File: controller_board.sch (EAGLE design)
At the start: 44 parts, among them J1 FRSKY-GIMBAL, J12 JST_3PIN_GND_VDD_SIG, J14 JST_3PIN_GND_VDD_SIG, J16 JST_3PIN_GND_VDD_SIG, J18 JST_3PIN_GND_VDD_SIG, J2 FRSKY-GIMBAL, J3 WIRE-HARNESS-SPARKFUN-9915, J6 HEADER-0.1IN-6POS-SCREW, J7 HEADER-0.1IN-6POS-FEMALE

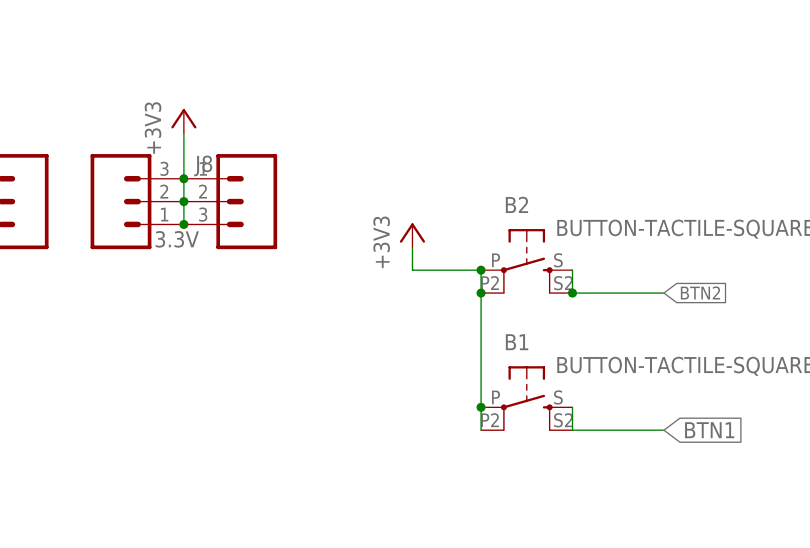
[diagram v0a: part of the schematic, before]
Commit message: fix polarity on butons.  Connect unconnected pin on batgnd breakouts
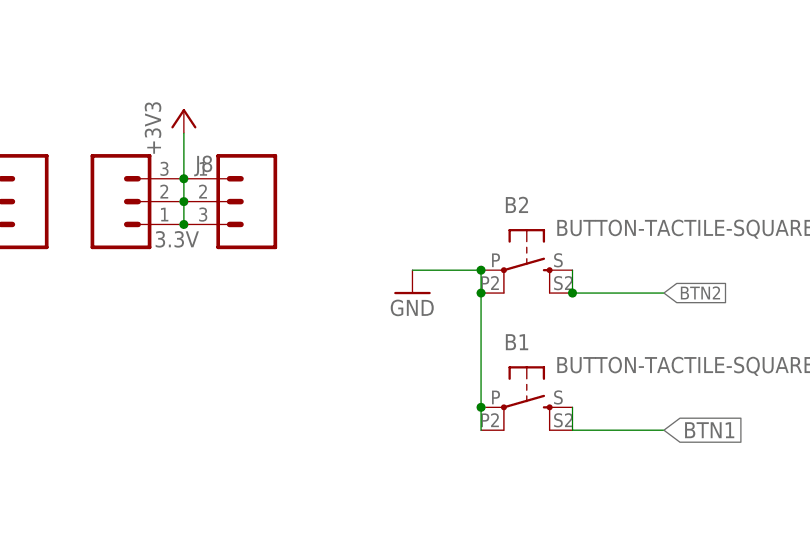
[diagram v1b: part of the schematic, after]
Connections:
- net +3V3: no longer B1.P, B1.P1, B2.P, B2.P1
- net GND: now also B1.P, B1.P1, B2.P, B2.P1
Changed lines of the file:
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@@
 <part name="D1" library="Components" deviceset="LED" device="3MM"/>
 <part name="B2" library="Controller" deviceset="BUTTON-TACTILE" device="-SQUARE"/>
-<part name="+3V6" library="supply1" deviceset="+3V3" device=""/>
 <part name="GND" library="Components" deviceset="HEADER-0.1IN-3POS" device="-SCREW">
 <attribute name="PIN1" value=""/>
@@
 <part name="GND9" library="supply1" deviceset="GND" device=""/>
 <part name="GND12" library="supply1" deviceset="GND" device=""/>
+<part name="GND10" library="supply1" deviceset="GND" device=""/>
 </parts>
 <sheets>
@@
 <instance part="D1" gate="G$1" x="-22.86" y="-17.78"/>
 <instance part="B2" gate="G$1" x="86.36" y="124.46" rot="R270"/>
-<instance part="+3V6" gate="G$1" x="73.66" y="129.54"/>
 <instance part="GND" gate="G$1" x="-15.24" y="127"/>
 <instance part="VBAT" gate="G$1" x="12.7" y="127"/>
@@
 <instance part="GND9" gate="1" x="167.64" y="17.78"/>
 <instance part="GND12" gate="1" x="157.48" y="17.78"/>
+<instance part="GND10" gate="1" x="73.66" y="121.92"/>
 </instances>
 <busses>
@@
 <wire x1="157.48" y1="30.48" x2="157.48" y2="20.32" width="0.1524" layer="91"/>
 </segment>
+<segment>
+<pinref part="B1" gate="G$1" pin="P1"/>
+<pinref part="B2" gate="G$1" pin="P1"/>
+<pinref part="B2" gate="G$1" pin="P"/>
+<wire x1="81.28" y1="124.46" x2="81.28" y2="121.92" width="0.1524" layer="91"/>
+<junction x="81.28" y="121.92"/>
+<pinref part="B1" gate="G$1" pin="P"/>
+<wire x1="81.28" y1="109.22" x2="81.28" y2="121.92" width="0.1524" layer="91"/>
+<junction x="81.28" y="109.22"/>
+<wire x1="81.28" y1="109.22" x2="81.28" y2="106.68" width="0.1524" layer="91"/>
+<wire x1="81.28" y1="124.46" x2="73.66" y2="124.46" width="0.1524" layer="91"/>
+<junction x="81.28" y="124.46"/>
+<pinref part="GND10" gate="1" pin="GND"/>
+</segment>
 </net>
 <net name="BTN1" class="0">
@@
 </segment>
 <segment>
-<pinref part="B1" gate="G$1" pin="P1"/>
-<pinref part="B2" gate="G$1" pin="P1"/>
-<pinref part="B2" gate="G$1" pin="P"/>
-<wire x1="81.28" y1="124.46" x2="81.28" y2="121.92" width="0.1524" layer="91"/>
-<junction x="81.28" y="121.92"/>
-<pinref part="B1" gate="G$1" pin="P"/>
-<wire x1="81.28" y1="109.22" x2="81.28" y2="121.92" width="0.1524" layer="91"/>
-<junction x="81.28" y="109.22"/>
-<wire x1="81.28" y1="109.22" x2="81.28" y2="106.68" width="0.1524" layer="91"/>
-<wire x1="81.28" y1="124.46" x2="73.66" y2="124.46" width="0.1524" layer="91"/>
-<junction x="81.28" y="124.46"/>
-<wire x1="73.66" y1="124.46" x2="73.66" y2="127" width="0.1524" layer="91"/>
-<pinref part="+3V6" gate="G$1" pin="+3V3"/>
-</segment>
-<segment>

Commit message: fix polarity on butons.  Connect unconnected pin on batgnd breakouts
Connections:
- net BATGND: now also GND.2
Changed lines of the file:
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@@
 <pinref part="J10" gate="G$1" pin="3"/>
 <label x="-5.08" y="124.46" size="1.778" layer="95" rot="R270" xref="yes"/>
+<pinref part="GND" gate="G$1" pin="2"/>
 </segment>
 <segment>

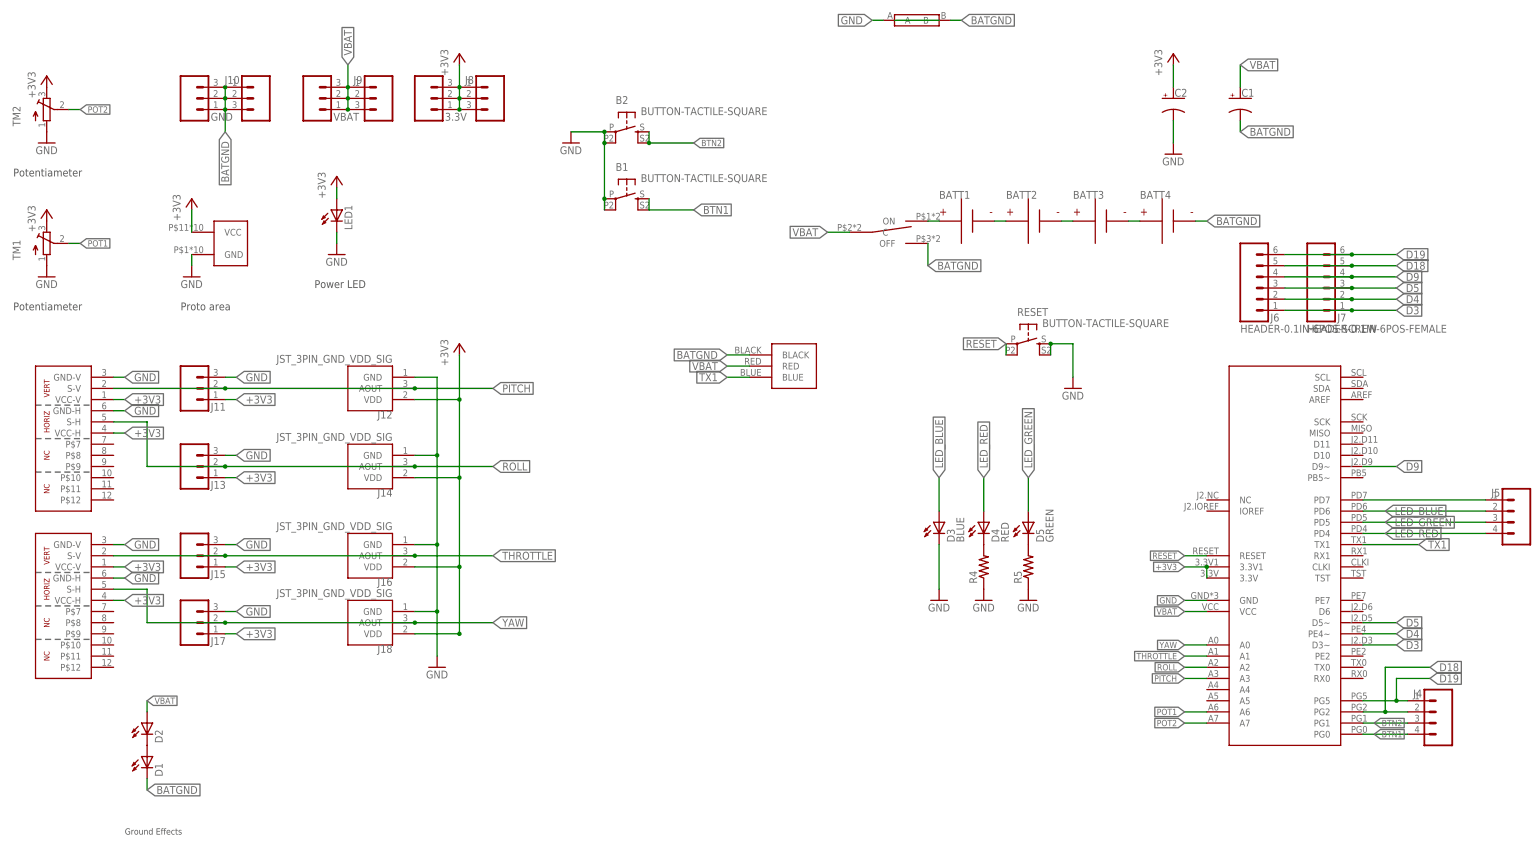
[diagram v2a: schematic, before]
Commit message: Connect AREF to 3.3V
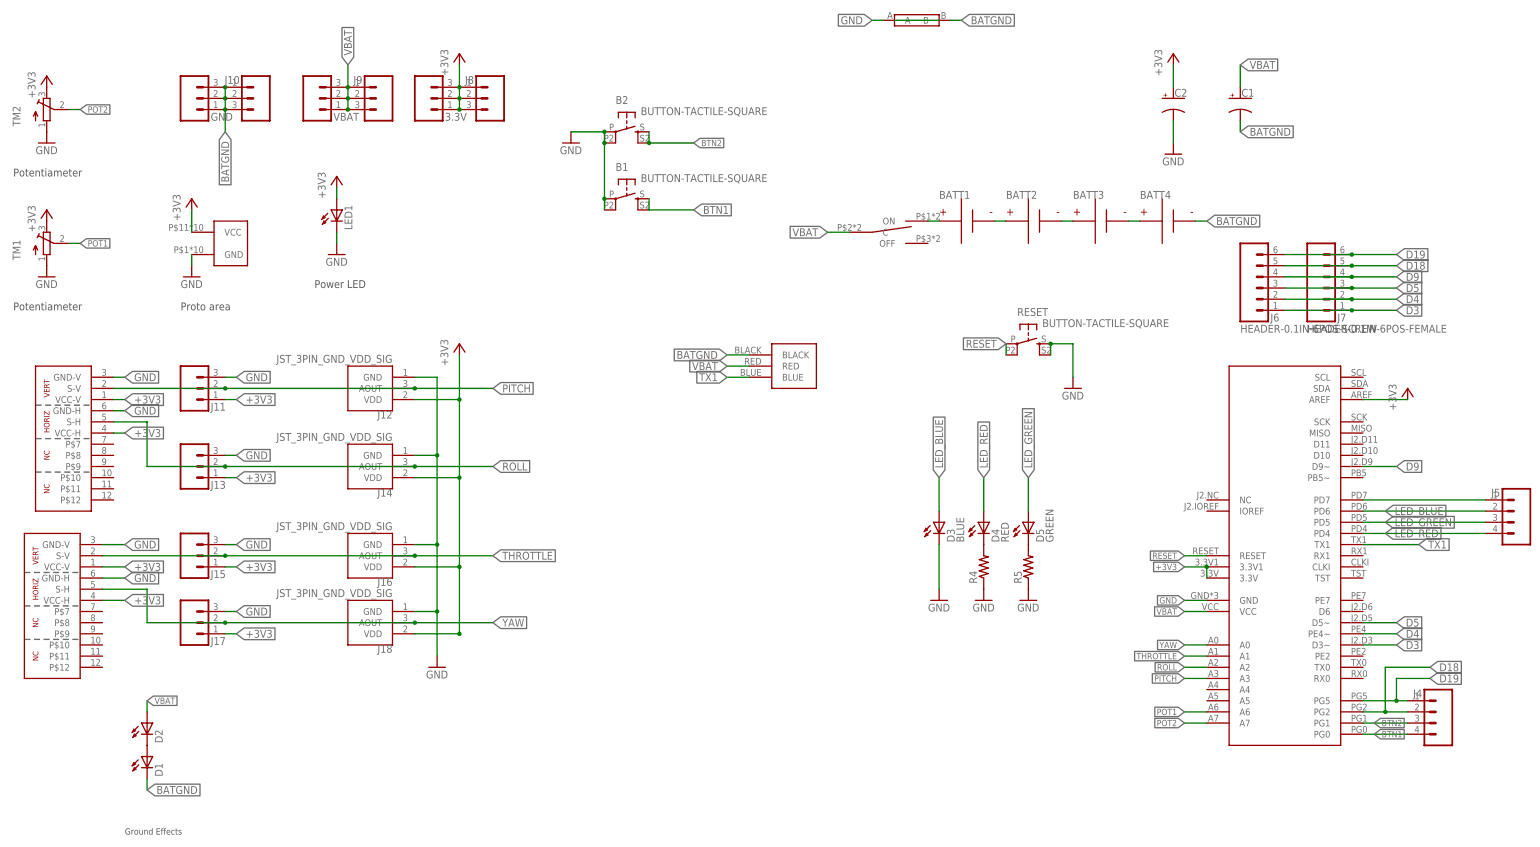
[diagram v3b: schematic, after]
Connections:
- net +3V3: now also U$4.AREF
- net BATGND: no longer S1.OFF
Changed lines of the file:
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@@
 <layer number="112" name="tSilk" color="7" fill="1" visible="yes" active="yes"/>
 <layer number="113" name="IDFDebug" color="4" fill="1" visible="yes" active="yes"/>
-<layer number="114" name="Unresolved" color="12" fill="1" visible="yes" active="yes"/>
-<layer number="115" name="Resolved" color="10" fill="1" visible="yes" active="yes"/>
-<layer number="116" name="Generic" color="9" fill="1" visible="yes" active="yes"/>
+<layer number="114" name="Unresolved" color="12" fill="1" visible="no" active="yes"/>
+<layer number="115" name="Resolved" color="10" fill="1" visible="no" active="yes"/>
+<layer number="116" name="Generic" color="9" fill="1" visible="no" active="yes"/>
 <layer number="11" name="Route11" color="4" fill="7" visible="no" active="no"/>
 <layer number="12" name="Route12" color="1" fill="5" visible="no" active="no"/>
@@
 <part name="GND12" library="supply1" deviceset="GND" device=""/>
 <part name="GND10" library="supply1" deviceset="GND" device=""/>
+<part name="+3V6" library="supply1" deviceset="+3V3" device=""/>
 </parts>
 <sheets>
@@
 <instance part="J15" gate="G$1" x="-15.24" y="22.86"/>
 <instance part="J17" gate="G$1" x="-15.24" y="7.62"/>
-<instance part="J2" gate="G$1" x="-33.02" y="5.08">
-<attribute name="CH1" x="-33.02" y="5.08" size="1.4224" layer="96" display="off"/>
-<attribute name="CH2" x="-33.02" y="5.08" size="1.4224" layer="96" display="off"/>
+<instance part="J2" gate="G$1" x="-35.56" y="5.08">
+<attribute name="CH1" x="-35.56" y="5.08" size="1.4224" layer="96" display="off"/>
+<attribute name="CH2" x="-35.56" y="5.08" size="1.4224" layer="96" display="off"/>
 </instance>
 <instance part="J1" gate="G$1" x="-33.02" y="43.18">
@@
 <instance part="GND12" gate="1" x="157.48" y="17.78"/>
 <instance part="GND10" gate="1" x="73.66" y="121.92"/>
+<instance part="+3V6" gate="G$1" x="264.16" y="66.04"/>
 </instances>
 <busses>
@@
 <segment>
 <pinref part="J2" gate="G$1" pin="GND-V"/>
-<wire x1="-30.48" y1="30.48" x2="-27.94" y2="30.48" width="0.1524" layer="91"/>
+<wire x1="-33.02" y1="30.48" x2="-27.94" y2="30.48" width="0.1524" layer="91"/>
 <label x="-27.94" y="30.48" size="1.778" layer="95" xref="yes"/>
 </segment>
 <segment>
 <pinref part="J2" gate="G$1" pin="GND-H"/>
-<wire x1="-30.48" y1="22.86" x2="-27.94" y2="22.86" width="0.1524" layer="91"/>
+<wire x1="-33.02" y1="22.86" x2="-27.94" y2="22.86" width="0.1524" layer="91"/>
 <label x="-27.94" y="22.86" size="1.778" layer="95" xref="yes"/>
 </segment>
@@
 <junction x="38.1" y="27.94"/>
 <pinref part="J2" gate="G$1" pin="S-V"/>
-<wire x1="-5.08" y1="27.94" x2="-30.48" y2="27.94" width="0.1524" layer="91"/>
+<wire x1="-5.08" y1="27.94" x2="-33.02" y2="27.94" width="0.1524" layer="91"/>
 <junction x="-5.08" y="27.94"/>
 </segment>
@@
 <junction x="-5.08" y="12.7"/>
 <pinref part="J2" gate="G$1" pin="S-H"/>
-<wire x1="-22.86" y1="20.32" x2="-30.48" y2="20.32" width="0.1524" layer="91"/>
+<wire x1="-22.86" y1="20.32" x2="-33.02" y2="20.32" width="0.1524" layer="91"/>
 </segment>
 <segment>
@@
 <segment>
 <pinref part="J2" gate="G$1" pin="VCC-V"/>
-<wire x1="-30.48" y1="25.4" x2="-27.94" y2="25.4" width="0.1524" layer="91"/>
+<wire x1="-33.02" y1="25.4" x2="-27.94" y2="25.4" width="0.1524" layer="91"/>
 <label x="-27.94" y="25.4" size="1.778" layer="95" xref="yes"/>
 </segment>
 <segment>
 <pinref part="J2" gate="G$1" pin="VCC-H"/>
-<wire x1="-30.48" y1="17.78" x2="-27.94" y2="17.78" width="0.1524" layer="91"/>
+<wire x1="-33.02" y1="17.78" x2="-27.94" y2="17.78" width="0.1524" layer="91"/>
 <label x="-27.94" y="17.78" size="1.778" layer="95" xref="yes"/>
 </segment>
@@
 <pinref part="+3V1" gate="G$1" pin="+3V3"/>
 </segment>
+<segment>
+<pinref part="U$4" gate="G$1" pin="AREF"/>
+<wire x1="254" y1="63.5" x2="264.16" y2="63.5" width="0.1524" layer="91"/>
+<pinref part="+3V6" gate="G$1" pin="+3V3"/>
+</segment>
 </net>
 <net name="TX1" class="0">
@@
 </segment>
 <segment>
-<pinref part="S1" gate="G$1" pin="OFF"/>
-<wire x1="154.94" y1="93.98" x2="154.94" y2="99.06" width="0.1524" layer="91"/>
-<label x="154.94" y="93.98" size="1.778" layer="95" xref="yes"/>
-</segment>
-<segment>
